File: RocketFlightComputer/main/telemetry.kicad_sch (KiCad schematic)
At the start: 2 parts

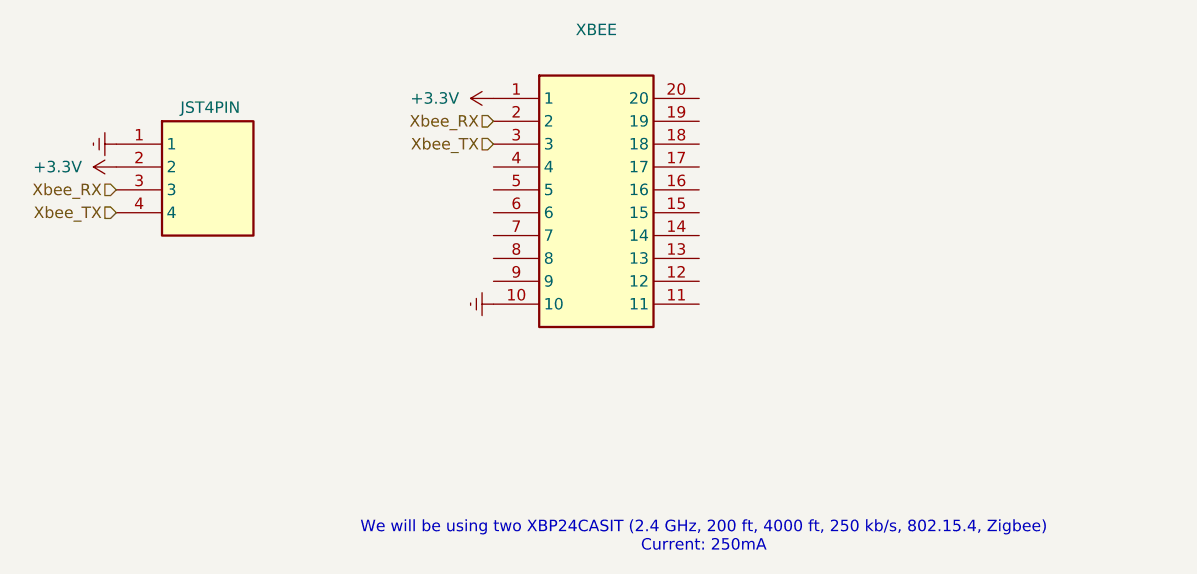
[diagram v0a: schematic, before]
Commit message: The design is getting more mature, still did not choose if doing 4 layers or 2 layers pcb, will try to add 5v for a on board camera and trace routes for reserved pins in case of usage on another vehicle
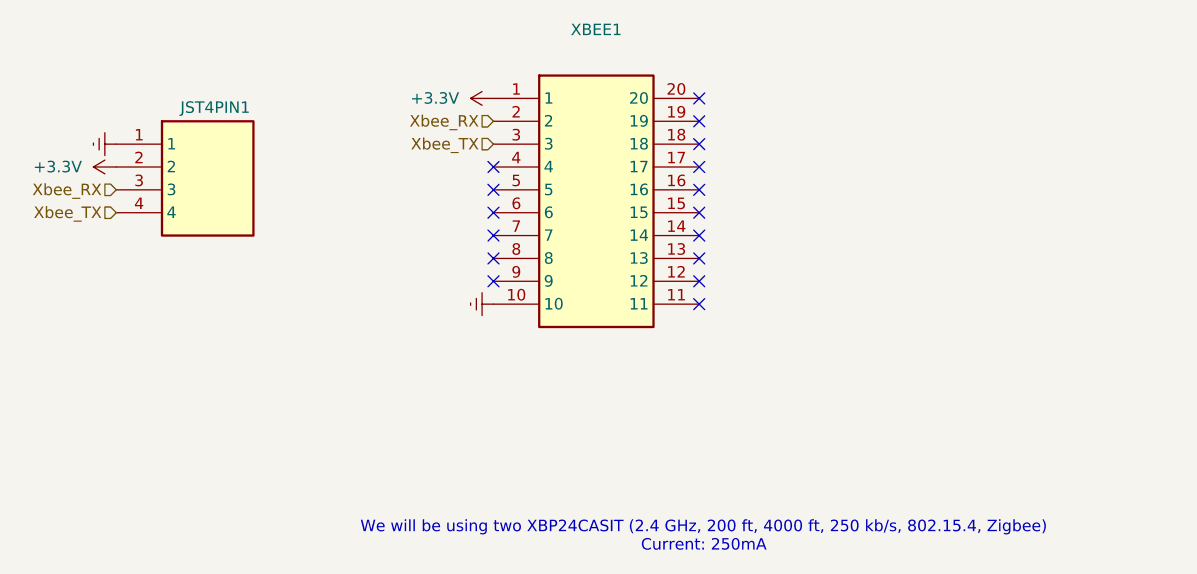
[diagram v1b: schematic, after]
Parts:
- renumbered JST4PIN to JST4PIN1, XBEE to XBEE1
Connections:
- no-connect marks 0 -> 16
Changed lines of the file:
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@@
 	(generator_version "8.0")
 	(paper "A5")
+	(no_connect
+		(at 139.7 62.23)
+	)
+	(no_connect
+		(at 116.84 67.31)
+	)
+	(no_connect
+		(at 139.7 74.93)
+	)
+	(no_connect
+		(at 139.7 57.15)
+	)
+	(no_connect
+		(at 139.7 67.31)
+	)
+	(no_connect
+		(at 139.7 64.77)
+	)
+	(no_connect
+		(at 139.7 59.69)
+	)
+	(no_connect
+		(at 139.7 54.61)
+	)
+	(no_connect
+		(at 139.7 52.07)
+	)
+	(no_connect
+		(at 139.7 69.85)
+	)
+	(no_connect
+		(at 116.84 62.23)
+	)
+	(no_connect
+		(at 116.84 72.39)
+	)
+	(no_connect
+		(at 116.84 69.85)
+	)
+	(no_connect
+		(at 139.7 72.39)
+	)
+	(no_connect
+		(at 116.84 64.77)
+	)
+	(no_connect
+		(at 116.84 59.69)
+	)
 	(text "We will be using two XBP24CASIT (2.4 GHz, 200 ft, 4000 ft, 250 kb/s, 802.15.4, Zigbee)\nCurrent: 250mA"
 		(exclude_from_sim no)
@@
 		(dnp no)
 		(fields_autoplaced yes)
-		(property "Reference" "XBEE"
+		(property "Reference" "XBEE1"
 			(at 128.27 44.45 0)
 			(effects
@@
 			(project ""
 				(path "/27195d1d-92b2-40df-ada5-3b20841577e7/e28c6e59-b6f8-4de5-b42d-020f37d4635d"
-					(reference "XBEE")
+					(reference "XBEE1")
 					(unit 1)
 				)
@@
 		(on_board yes)
 		(dnp no)
-		(property "Reference" "JST4PIN"
+		(property "Reference" "JST4PIN1"
 			(at 82.042 53.086 0)
 			(effects
@@
 			(project ""
 				(path "/27195d1d-92b2-40df-ada5-3b20841577e7/e28c6e59-b6f8-4de5-b42d-020f37d4635d"
-					(reference "JST4PIN")
+					(reference "JST4PIN1")
 					(unit 1)
 				)

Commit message: Camera and reserve
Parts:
- JST4PIN1: footprint footprint:S4B -> Connector_JST:JST_GH_BM04B-GHS-TBT_1x04-1MP_P1.25mm_Vertical
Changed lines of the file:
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@@
 			)
 		)
-		(property "Footprint" "footprint:S4B"
+		(property "Footprint" "Connector_JST:JST_GH_BM04B-GHS-TBT_1x04-1MP_P1.25mm_Vertical"
 			(at 91.44 152.07 0)
 			(effects

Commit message: Layout of PCB mostly done
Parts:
- S4B-PH-K-S_LF__SN_1: renamed from JST4PIN1; value S4B-PH-K-S_LF__SN_ -> TELEMETRY
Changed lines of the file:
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@@
 		(on_board yes)
 		(dnp no)
-		(property "Reference" "JST4PIN1"
-			(at 82.042 53.086 0)
-			(effects
-				(font
-					(size 1.27 1.27)
-				)
-				(justify left)
-			)
-		)
-		(property "Value" "S4B-PH-K-S_LF__SN_"
-			(at 91.44 62.2299 0)
+		(property "Reference" "S4B-PH-K-S_LF__SN_1"
+			(at 80.264 53.086 0)
 			(effects
 				(font
@@
 				(justify left)
 				(hide yes)
+			)
+		)
+		(property "Value" "TELEMETRY"
+			(at 79.756 52.832 0)
+			(effects
+				(font
+					(size 1.27 1.27)
+				)
+				(justify left)
 			)
 		)
@@
 			(project ""
 				(path "/27195d1d-92b2-40df-ada5-3b20841577e7/e28c6e59-b6f8-4de5-b42d-020f37d4635d"
-					(reference "JST4PIN1")
+					(reference "S4B-PH-K-S_LF__SN_1")
 					(unit 1)
 				)

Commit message: Addition of teensy example and milestone on routing completed, missing a few components to connect
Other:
- note added: "We will be using two XBP24CASIT (2.4 GHz, 200 ft, 4000 ft, 250 kb/s, 802.15.4, Zigbee) Current: 33mA"
- note removed: "We will be using two XBP24CASIT (2.4 GHz, 200 ft, 4000 ft, 250 kb/s, 802.15.4, Zigbee) Current: 250mA"
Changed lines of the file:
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@@
 		(at 116.84 59.69)
 	)
-	(text "We will be using two XBP24CASIT (2.4 GHz, 200 ft, 4000 ft, 250 kb/s, 802.15.4, Zigbee)\nCurrent: 250mA"
+	(text "We will be using two XBP24CASIT (2.4 GHz, 200 ft, 4000 ft, 250 kb/s, 802.15.4, Zigbee)\nCurrent: 33mA"
 		(exclude_from_sim no)
 		(at 140.208 100.838 0)

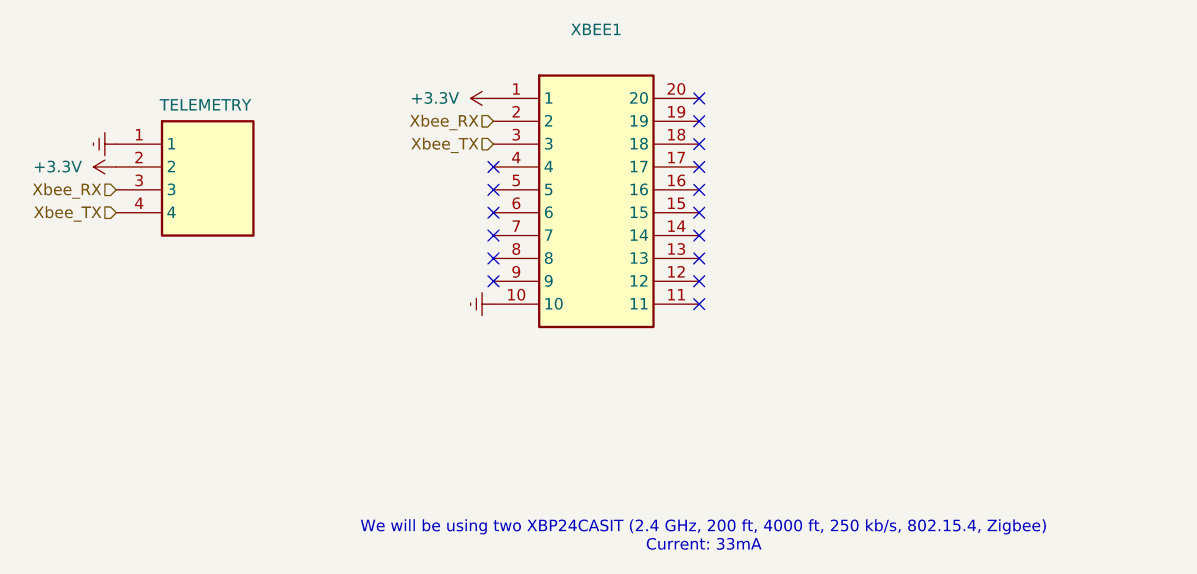
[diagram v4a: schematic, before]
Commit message: PR1; Fix PSRAM length of data, clock and cs pins to match since high speed data transmission, needs to be within 0.5mm trace length delta
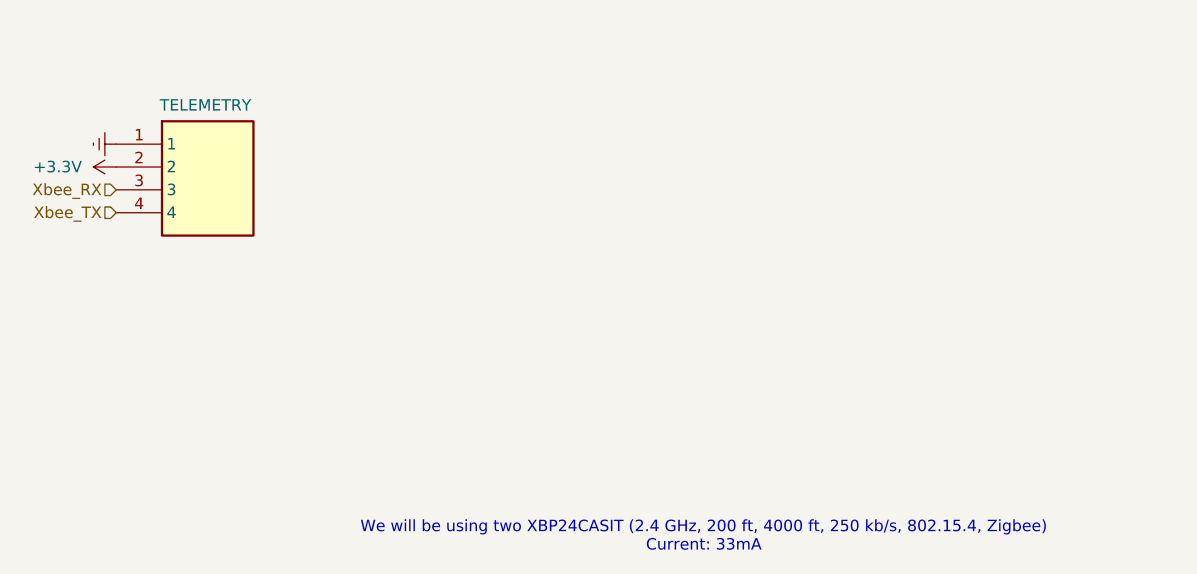
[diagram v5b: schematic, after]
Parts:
- removed XBEE1: XB24CAPIT-001, footprint:XB24CAPIT-001, symbol XBEE:XB24CAPIT-001
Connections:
- no-connect marks 16 -> 0

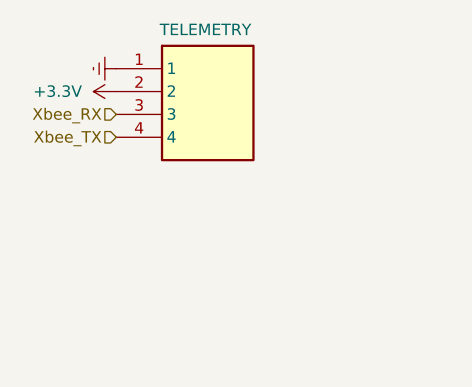
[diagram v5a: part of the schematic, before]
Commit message: First pass of verification and validation of pcb design
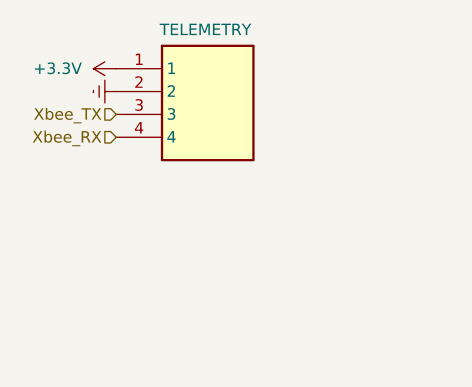
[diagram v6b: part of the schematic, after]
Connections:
- net +3.3V: now also S4B-PH-K-S_LF__SN_1.1; no longer S4B-PH-K-S_LF__SN_1.2
- net GNDREF: now also S4B-PH-K-S_LF__SN_1.2; no longer S4B-PH-K-S_LF__SN_1.1
- net Xbee_RX: now also S4B-PH-K-S_LF__SN_1.4; no longer S4B-PH-K-S_LF__SN_1.3
- net Xbee_TX: now also S4B-PH-K-S_LF__SN_1.3; no longer S4B-PH-K-S_LF__SN_1.4
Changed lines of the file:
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@@
 		)
 	)
-	(hierarchical_label "Xbee_RX"
+	(hierarchical_label "Xbee_TX"
 		(shape input)
 		(at 74.93 62.23 180)
@@
 		)
 	)
-	(hierarchical_label "Xbee_TX"
+	(hierarchical_label "Xbee_RX"
 		(shape input)
 		(at 74.93 64.77 180)
@@
 	(symbol
 		(lib_id "power:+3.3V")
-		(at 74.93 59.69 90)
+		(at 74.93 57.15 90)
 		(unit 1)
 		(exclude_from_sim no)
@@
 		(dnp no)
 		(fields_autoplaced yes)
-		(property "Reference" "#PWR0142"
-			(at 78.74 59.69 0)
+		(property "Reference" "#PWR076"
+			(at 78.74 57.15 0)
 			(effects
 				(font
@@
 		)
 		(property "Value" "+3.3V"
-			(at 71.12 59.6899 90)
+			(at 71.12 57.1499 90)
 			(effects
 				(font
@@
 				)
 				(justify left)
+			)
+		)
+		(property "Footprint" ""
+			(at 74.93 57.15 0)
+			(effects
+				(font
+					(size 1.27 1.27)
+				)
+				(hide yes)
+			)
+		)
+		(property "Datasheet" ""
+			(at 74.93 57.15 0)
+			(effects
+				(font
+					(size 1.27 1.27)
+				)
+				(hide yes)
+			)
+		)
+		(property "Description" ""
+			(at 74.93 57.15 0)
+			(effects
+				(font
+					(size 1.27 1.27)
+				)
+				(hide yes)
+			)
+		)
+		(pin "1"
+		)
+		(instances
+			(project "main"
+				(path "/27195d1d-92b2-40df-ada5-3b20841577e7/e28c6e59-b6f8-4de5-b42d-020f37d4635d"
+					(reference "#PWR076")
+					(unit 1)
+				)
+			)
+		)
+	)
+	(symbol
+		(lib_id "power:GNDREF")
+		(at 74.93 59.69 270)
+		(unit 1)
+		(exclude_from_sim no)
+		(in_bom yes)
+		(on_board yes)
+		(dnp no)
+		(fields_autoplaced yes)
+		(property "Reference" "#PWR096"
+			(at 68.58 59.69 0)
+			(effects
+				(font
+					(size 1.27 1.27)
+				)
+				(hide yes)
+			)
+		)
+		(property "Value" "GNDREF"
+			(at 71.12 59.055 90)
+			(effects
+				(font
+					(size 1.27 1.27)
+				)
+				(justify right)
+				(hide yes)
 			)
 		)
@@
 			(project "main"
 				(path "/27195d1d-92b2-40df-ada5-3b20841577e7/e28c6e59-b6f8-4de5-b42d-020f37d4635d"
-					(reference "#PWR0142")
+					(reference "#PWR096")
 					(unit 1)
 				)
-			)
-		)
-	)
-	(symbol
-		(lib_id "power:GNDREF")
-		(at 74.93 57.15 270)
-		(unit 1)
-		(exclude_from_sim no)
-		(in_bom yes)
-		(on_board yes)
-		(dnp no)
-		(fields_autoplaced yes)
-		(property "Reference" "#PWR0143"
-			(at 68.58 57.15 0)
-			(effects
-				(font
-					(size 1.27 1.27)
-				)
-				(hide yes)
-			)
-		)
-		(property "Value" "GNDREF"
-			(at 71.12 56.515 90)
-			(effects
-				(font
-					(size 1.27 1.27)
-				)
-				(justify right)
-				(hide yes)
-			)
-		)
-		(property "Footprint" ""
-			(at 74.93 57.15 0)
-			(effects
-				(font
-					(size 1.27 1.27)
-				)
-				(hide yes)
-			)
-		)
-		(property "Datasheet" ""
-			(at 74.93 57.15 0)
-			(effects
-				(font
-					(size 1.27 1.27)
-				)
-				(hide yes)
-			)
-		)
-		(property "Description" ""
-			(at 74.93 57.15 0)
-			(effects
-				(font
-					(size 1.27 1.27)
-				)
-				(hide yes)
-			)
-		)
-		(pin "1"
-		)
-		(instances
-			(project "main"
-				(path "/27195d1d-92b2-40df-ada5-3b20841577e7/e28c6e59-b6f8-4de5-b42d-020f37d4635d"
-					(reference "#PWR0143")
-					(unit 1)
-				)

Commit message: Addition of all components in BOM, metal mounting plates, need to check psram if its ok for signals to pass under, all components need a double check
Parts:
- S4B-PH-K-S_LF__SN_1: LCSC (none) -> C161692; Mouser Part Number N/A -> 306-BM04BGHSTBTLFSNN
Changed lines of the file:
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@@
 		(dnp no)
 		(fields_autoplaced yes)
-		(property "Reference" "#PWR076"
+		(property "Reference" "#PWR0137"
 			(at 78.74 57.15 0)
 			(effects
@@
 			(project "main"
 				(path "/27195d1d-92b2-40df-ada5-3b20841577e7/e28c6e59-b6f8-4de5-b42d-020f37d4635d"
-					(reference "#PWR076")
+					(reference "#PWR0137")
 					(unit 1)
 				)
@@
 		(dnp no)
 		(fields_autoplaced yes)
-		(property "Reference" "#PWR096"
+		(property "Reference" "#PWR0138"
 			(at 68.58 59.69 0)
 			(effects
@@
 			(project "main"
 				(path "/27195d1d-92b2-40df-ada5-3b20841577e7/e28c6e59-b6f8-4de5-b42d-020f37d4635d"
-					(reference "#PWR096")
+					(reference "#PWR0138")
 					(unit 1)
 				)
@@
 			)
 		)
-		(property "Mouser Part Number" "N/A"
+		(property "Mouser Part Number" "306-BM04BGHSTBTLFSNN"
 			(at 91.44 552.07 0)
 			(effects
@@
 				(hide yes)
 			)
+		)
+		(property "LCSC" "C161692"
+			(at 74.93 57.15 0)
+			(effects
+				(font
+					(size 1.27 1.27)
+				)
+				(hide yes)
+			)
